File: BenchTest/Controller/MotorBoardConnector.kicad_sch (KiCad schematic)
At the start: 21 parts, among them J8 Conn_01x10, U1 TLP2355(TPL,E, U2 TLP2355(TPL,E, U3 TLP2355(TPL,E, U4 TLP2355(TPL,E, U5 TLP2355(TPL,E, U6 TLP2355(TPL,E

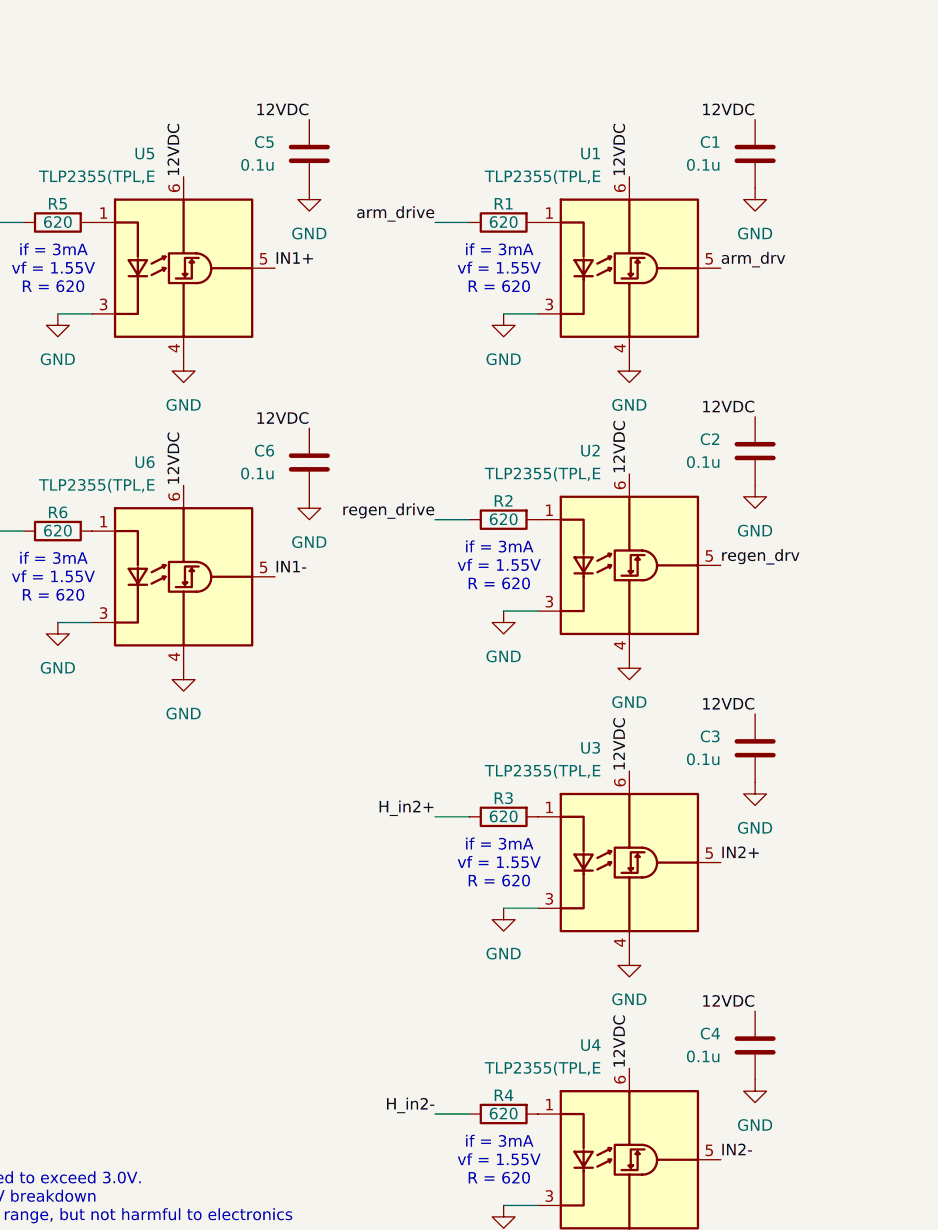
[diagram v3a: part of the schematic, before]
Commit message: Migrated to 5V drive from digital side
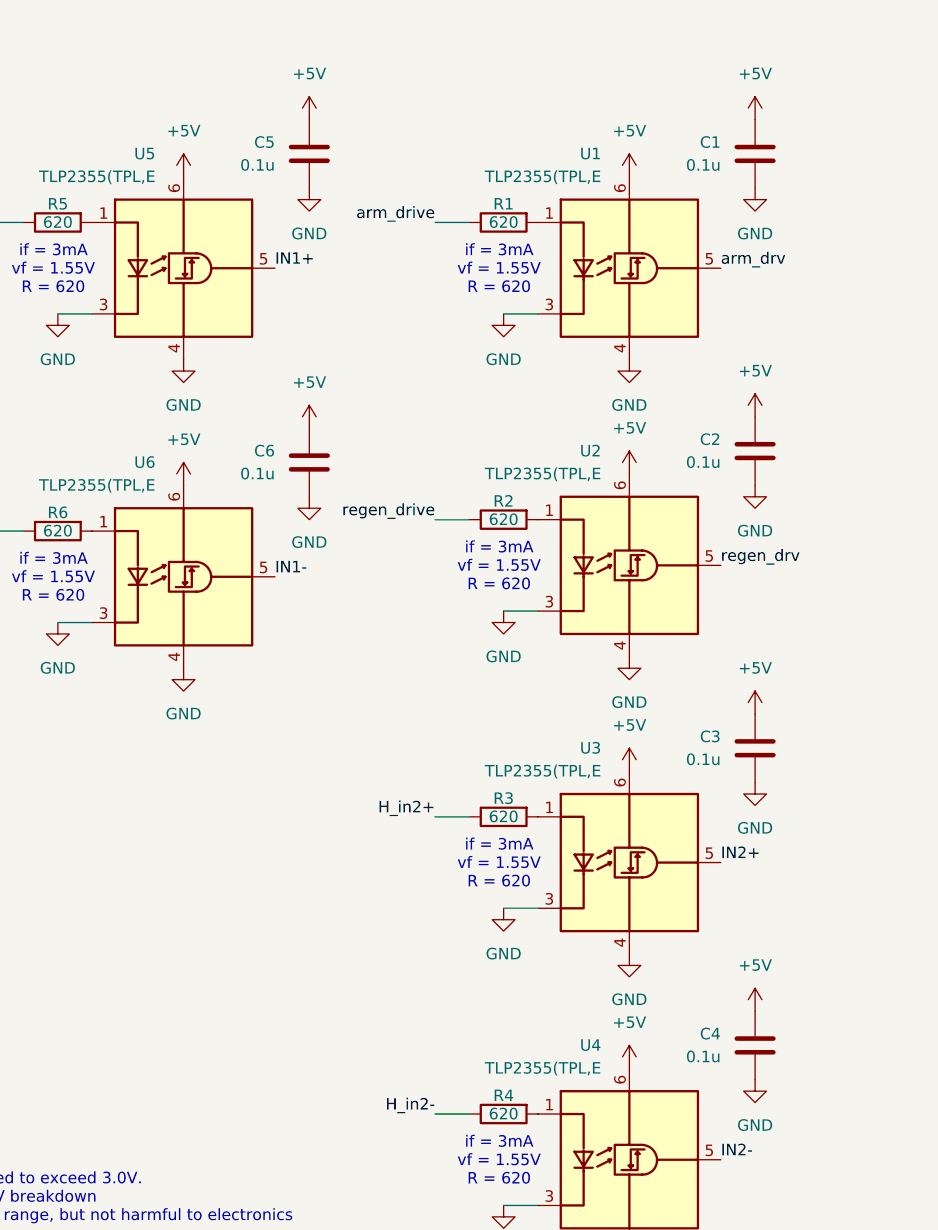
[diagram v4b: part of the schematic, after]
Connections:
- net 12VDC renamed +5V
